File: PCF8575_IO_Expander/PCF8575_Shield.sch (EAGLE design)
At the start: 19 parts

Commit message: Added OLED Shield Added LiPo Battery Charger Shield Updated outlines of all shields to match the cutout of the nodemcu board
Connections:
- net GND: no longer U$2.MO/MOSI/SDCMD
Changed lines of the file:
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@@
 <parts>
 <part name="GND1" library="SparkFun" deviceset="GND" device=""/>
-<part name="GND2" library="SparkFun" deviceset="GND" device=""/>
 <part name="GND4" library="SparkFun" deviceset="GND" device=""/>
 <part name="C1" library="SparkFun" deviceset="CAP" device="0603-CAP" value=".1uF"/>
@@
 <instances>
 <instance part="GND1" gate="1" x="101.6" y="40.64"/>
-<instance part="GND2" gate="1" x="-43.18" y="53.34"/>
 <instance part="GND4" gate="1" x="157.48" y="91.44"/>
 <instance part="C1" gate="G$1" x="157.48" y="99.06"/>
@@
 </segment>
 <segment>
-<pinref part="GND2" gate="1" pin="GND"/>
-<pinref part="U$2" gate="G$1" pin="MO/MOSI/SDCMD"/>
-</segment>
-<segment>

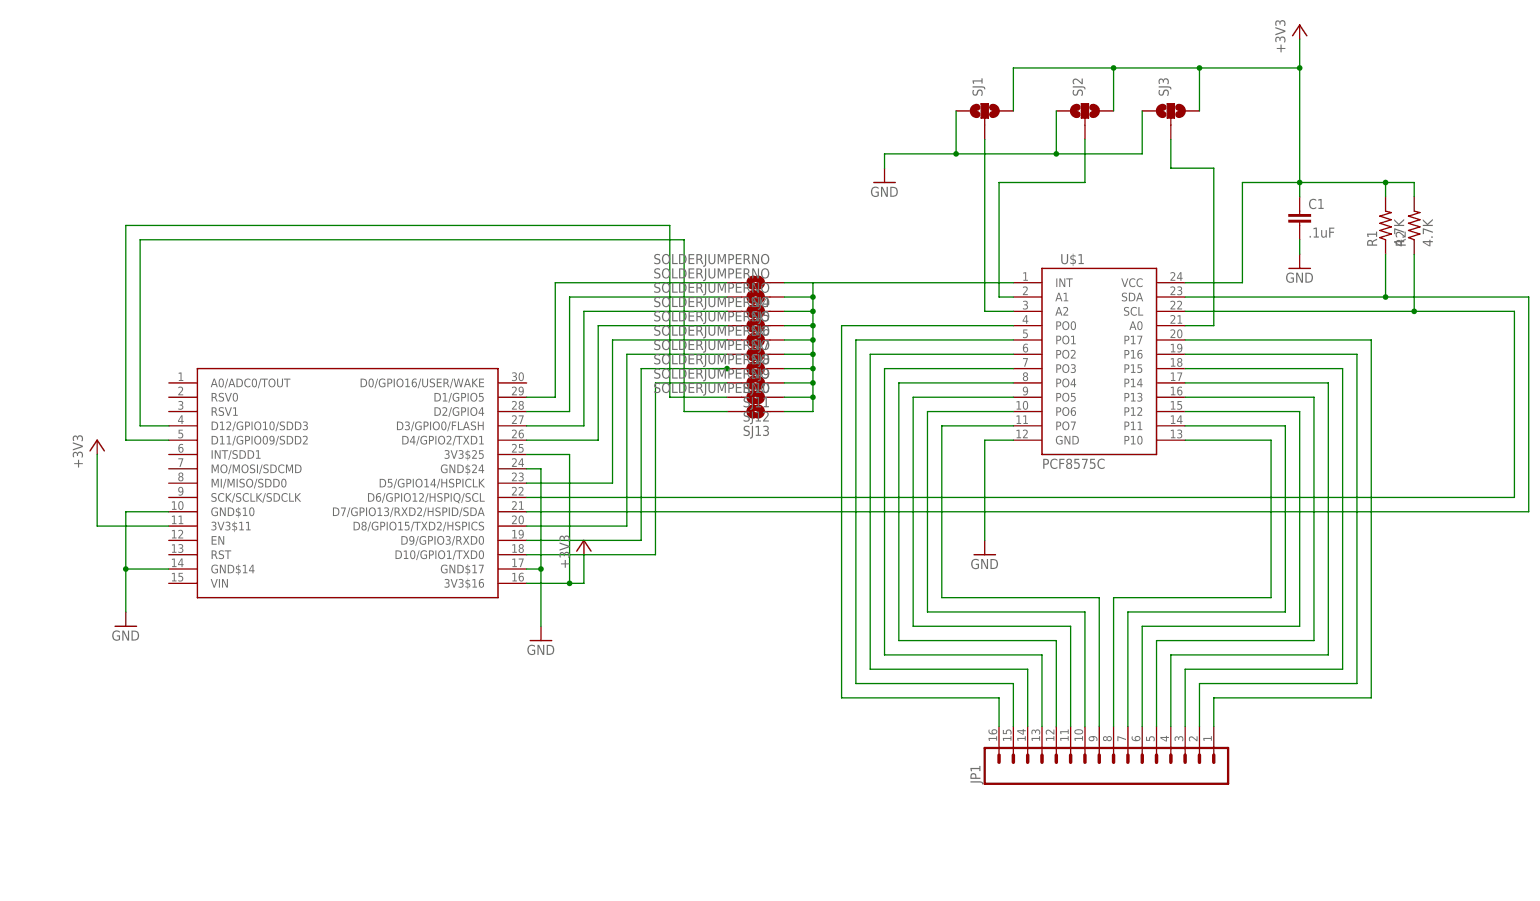
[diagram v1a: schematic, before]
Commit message: Updated the i2c pins to all shields to use d11/d12  as these pins will have dual use with the upcoming wifimcu Added FM24W256  Fram shield Added X95840 Digital potentiometer Shield Added AD5696 DAC Shield
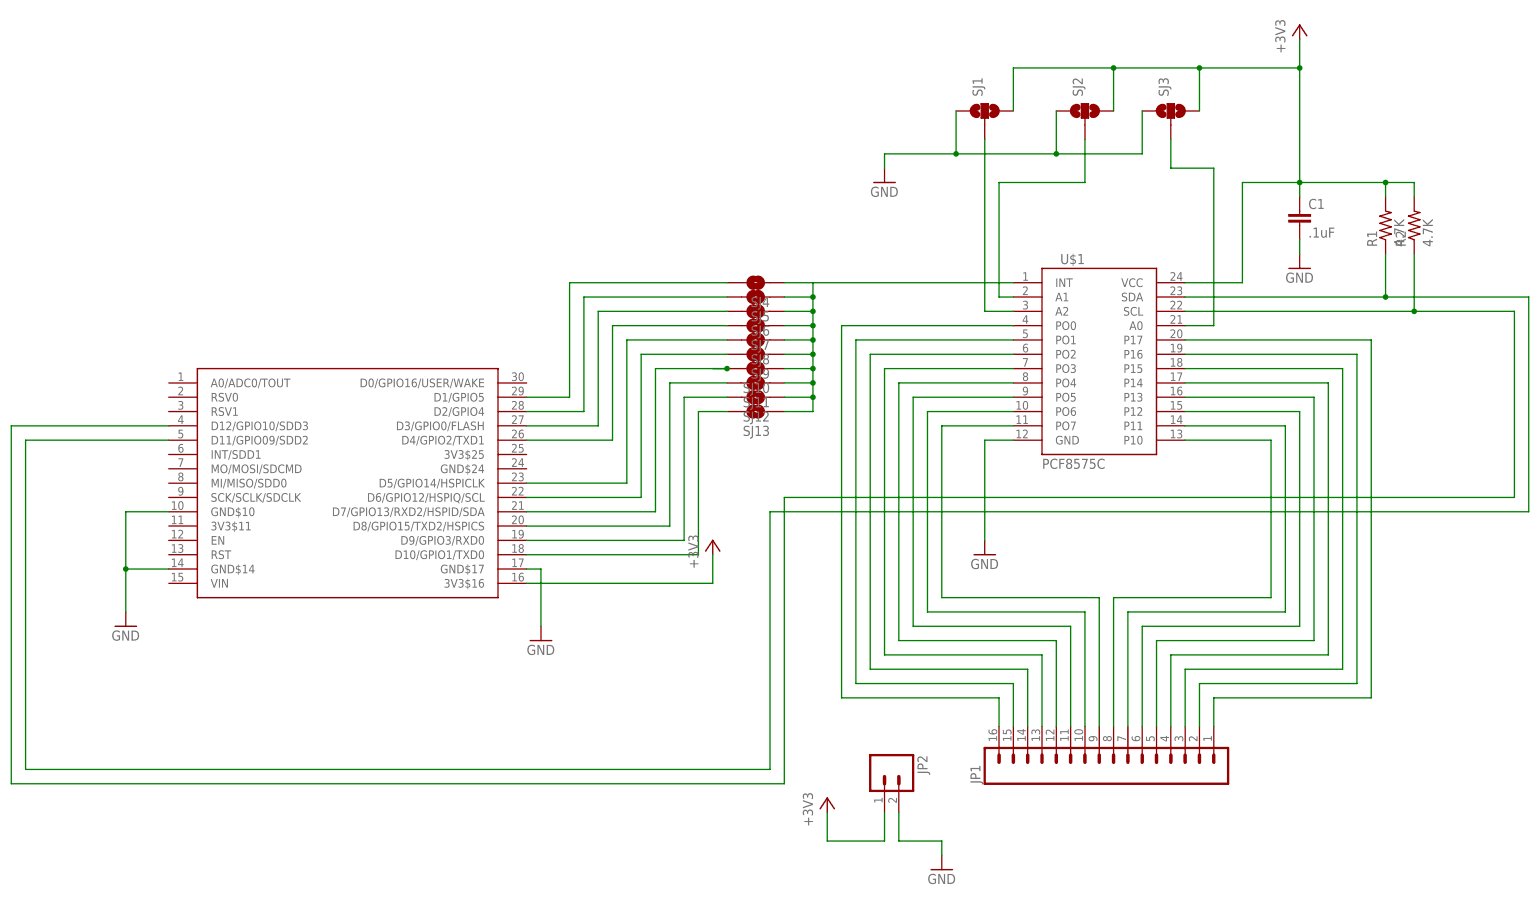
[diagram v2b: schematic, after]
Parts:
- added JP2: (no value), SparkFun:M02PTH
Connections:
- net +3V3: now also JP2.1; no longer U$2.3V3$11, U$2.3V3$25
- net GND: now also JP2.2; no longer U$2.GND$24
- net N$2: now also U$2.D11/GPIO09/SDD2; no longer U$2.D7/GPIO13/RXD2/HSPID/SDA
- net N$28: now also U$2.D6/GPIO12/HSPIQ/SCL; no longer U$2.D8/GPIO15/TXD2/HSPICS
- net N$29: now also U$2.D7/GPIO13/RXD2/HSPID/SDA; no longer U$2.D9/GPIO3/RXD0
- net N$30: now also U$2.D8/GPIO15/TXD2/HSPICS; no longer U$2.D10/GPIO1/TXD0
- net N$31: now also U$2.D9/GPIO3/RXD0; no longer U$2.D11/GPIO09/SDD2
- net N$32: now also U$2.D10/GPIO1/TXD0; no longer U$2.D12/GPIO10/SDD3
- net N$5: now also U$2.D12/GPIO10/SDD3; no longer U$2.D6/GPIO12/HSPIQ/SCL
